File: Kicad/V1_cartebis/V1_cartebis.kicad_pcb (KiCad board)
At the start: 2 copper layers, 79 parts, among them J1 Conn_01x05_Pin, J10 Conn_01x02_Pin, J11 Conn_01x02_Pin, J12 Conn_01x02_Pin, J13 Conn_01x02_Pin, J14 Conn_01x02_Pin, J15 Conn_01x02_Pin, J16 Conn_01x02_Pin, J17 Conn_01x02_Pin, J18 Conn_01x02_Pin, J19 Conn_01x02_Pin, J2 Conn_01x02_Pin, J20 Conn_01x02_Pin, J21 Conn_01x02_Pin, J22 Conn_01x02_Pin, J23 Conn_01x02_Pin, J24 Conn_01x02_Pin, J25 Conn_01x02_Pin, J26 Conn_01x02_Pin, J27 Conn_01x02_Pin, J28 Conn_01x02_Pin, J29 Conn_01x02_Pin, J3 Conn_01x02_Pin, J30 Conn_01x02_Pin, J31 Conn_01x02_Pin, J32 Conn_01x05_Pin, J33 Conn_01x01_Pin, J34 Conn_01x01_Pin, J35 Conn_01x01_Pin, J36 Conn_01x03_Pin, J37 Conn_01x03_Pin, J38 Conn_01x03_Pin, J39 Conn_01x03_Pin, J4 Conn_01x02_Pin, J40 Conn_01x01_Pin, J41 Conn_01x01_Pin, J42 Conn_01x01_Pin, J5 Conn_01x02_Pin, J6 Conn_01x02_Pin, J7 Conn_01x02_Pin, J8 Conn_01x02_Pin, J9 Conn_01x02_Pin, U1 MCP23020-E/SO, U10 ISOM11600DFGR, U11 ISOM11600DFGR, U12 ISOM11600DFGR, U13 ISOM11600DFGR, U14 ISOM11600DFGR, U15 ISOM11600DFGR, U16 ISOM11600DFGR, U17 ISOM11600DFGR, U18 P82B715DRG4, U2 LTC24127CUHF-TRPBF, U3 ISOM11600DFGR, U4 ISOM11600DFGR, U5 ISOM11600DFGR, U6 ISOM11600DFGR, U7 ISOM11600DFGR, U8 ISOM11600DFGR, U9 ISOM11600DFGR

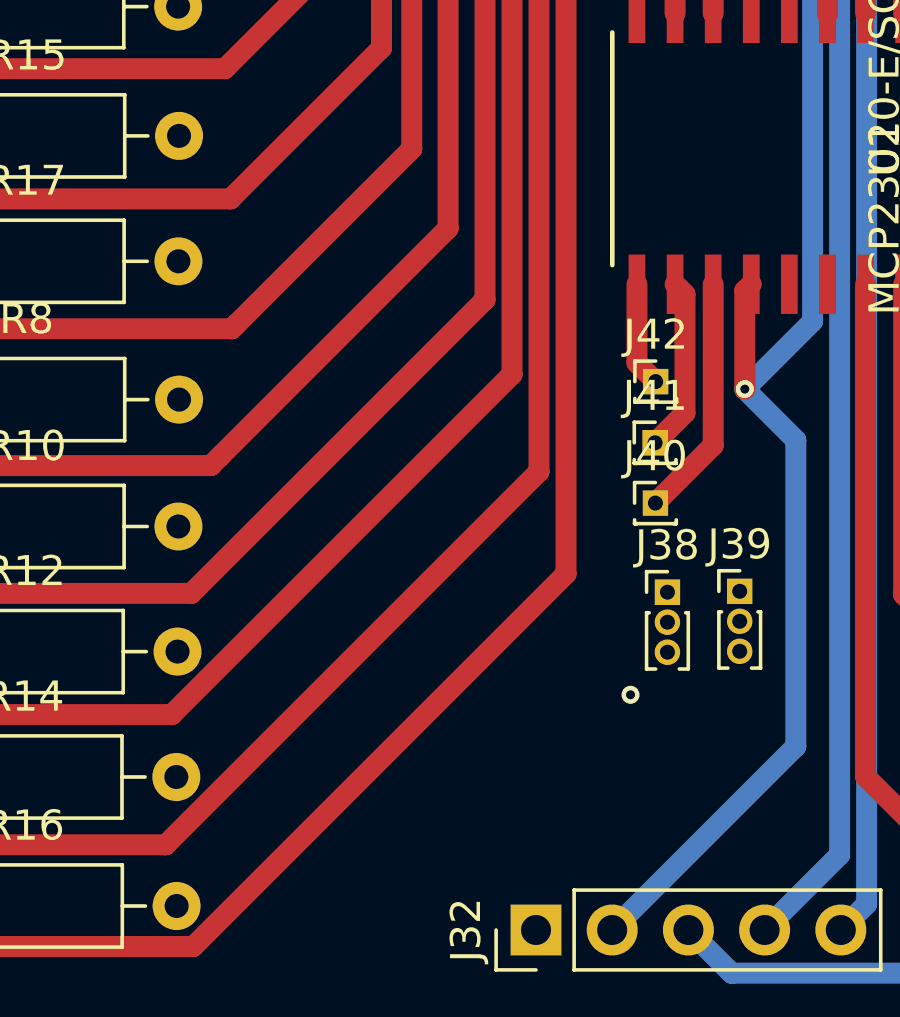
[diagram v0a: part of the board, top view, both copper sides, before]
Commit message: fonction I2C SPS30
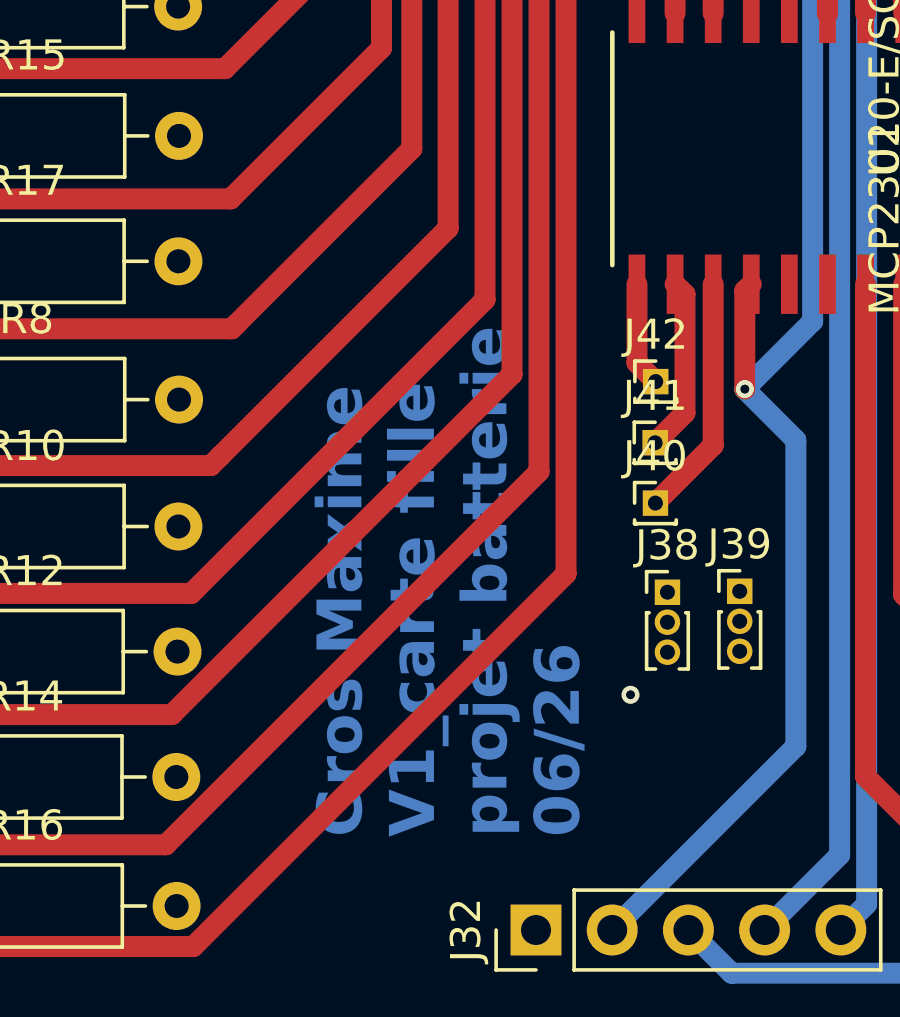
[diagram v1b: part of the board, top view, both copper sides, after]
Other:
- board text added: "Gros Maxime V1_carte fille projet batterie 06/26"
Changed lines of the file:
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@@
       (outputformat 1)
       (mirror false)
-      (drillshape 1)
+      (drillshape 0)
       (scaleselection 1)
-      (outputdirectory "")
+      (outputdirectory "/home/xoum/stage_recup/Kicad/Percage carte fille/")
     )
   )
@@
     (effects (font (size 0.5 0.5) (thickness 0.125) bold) (justify left bottom))
   )
+  (gr_text "Gros Maxime\nV1_carte fille\nprojet batterie\n06/26" (at 162.8 96.35 90) (layer "B.Cu")
+    (effects (font (size 1.5 1.5) (thickness 0.3) bold) (justify left bottom))
+  )
   (segment (start 166.939999 61.250001) (end 167.11 61.08) (width 0.2) (layer "F.Cu") (net 1))
